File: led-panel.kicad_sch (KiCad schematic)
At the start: 4 parts

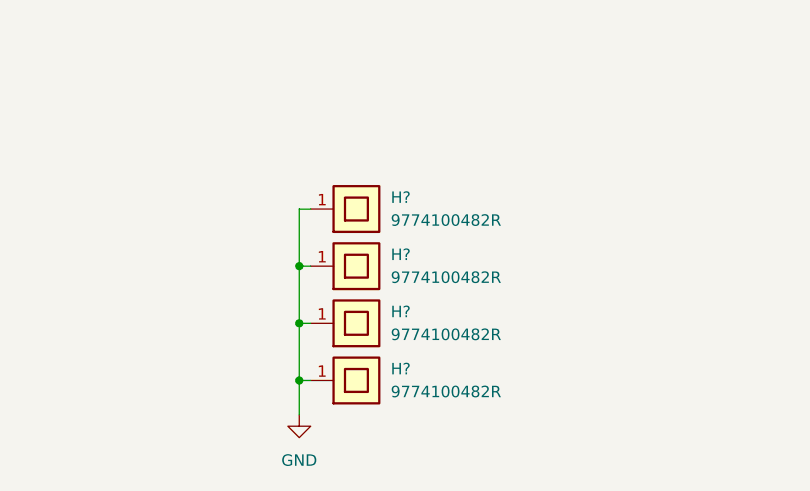
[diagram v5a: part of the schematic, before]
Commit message: [#72133] Change connectors to horizontal
Signed-off-by: Dawid Lentka <dlentka@antmicro.com>
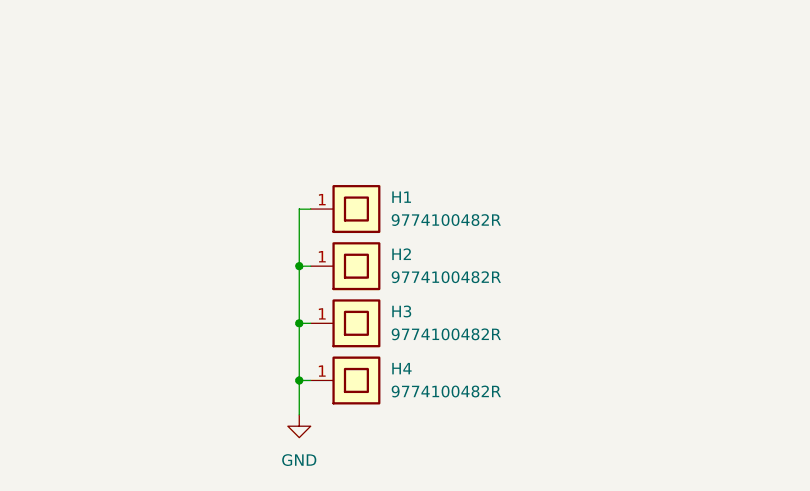
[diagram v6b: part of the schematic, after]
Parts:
- gave numbers to parts that had none: 4
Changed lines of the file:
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@@
 		(dnp no)
 		(fields_autoplaced yes)
-		(property "Reference" "H?"
+		(property "Reference" "H3"
 			(at 160.02 179.07 0)
 			(effects
@@
 			(project "led-panel"
 				(path "/a86e1cab-ea0a-45e6-9194-d44b0d5c9450"
-					(reference "H?")
+					(reference "H3")
 					(unit 1)
 				)
@@
 		(dnp no)
 		(fields_autoplaced yes)
-		(property "Reference" "H?"
+		(property "Reference" "H1"
 			(at 160.02 166.37 0)
 			(effects
@@
 			(project ""
 				(path "/a86e1cab-ea0a-45e6-9194-d44b0d5c9450"
-					(reference "H?")
+					(reference "H1")
 					(unit 1)
 				)
@@
 		(dnp no)
 		(fields_autoplaced yes)
-		(property "Reference" "H?"
+		(property "Reference" "H4"
 			(at 160.02 185.42 0)
 			(effects
@@
 			(project "led-panel"
 				(path "/a86e1cab-ea0a-45e6-9194-d44b0d5c9450"
-					(reference "H?")
+					(reference "H4")
 					(unit 1)
 				)
@@
 		(dnp no)
 		(fields_autoplaced yes)
-		(property "Reference" "H?"
+		(property "Reference" "H2"
 			(at 160.02 172.72 0)
 			(effects
@@
 			(project "led-panel"
 				(path "/a86e1cab-ea0a-45e6-9194-d44b0d5c9450"
-					(reference "H?")
+					(reference "H2")
 					(unit 1)
 				)

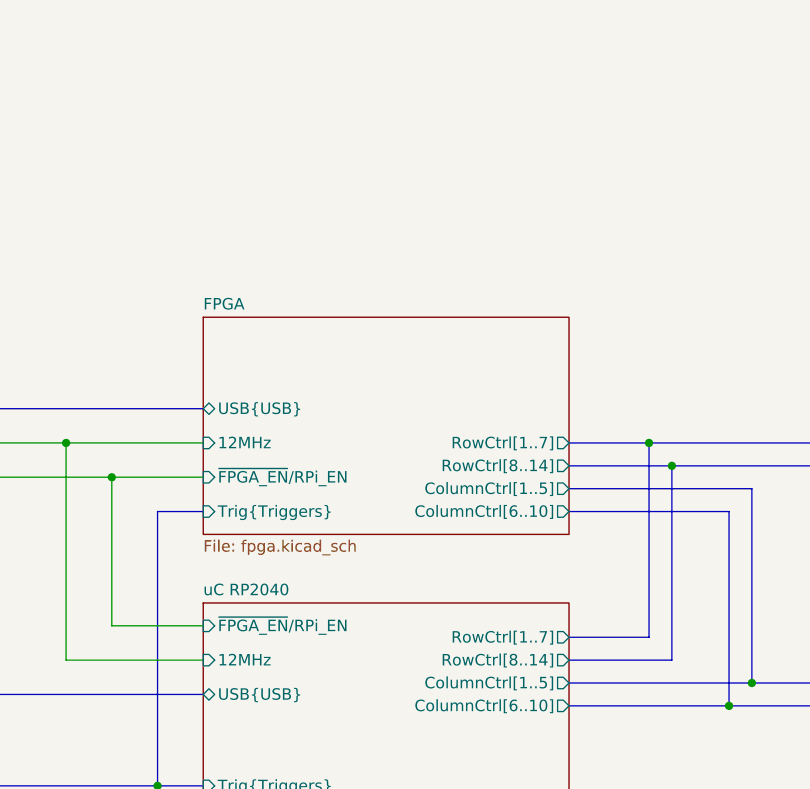
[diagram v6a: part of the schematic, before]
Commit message: [#72133] Sch: Add IMU
Signed-off-by: Dawid Lentka <dlentka@antmicro.com>
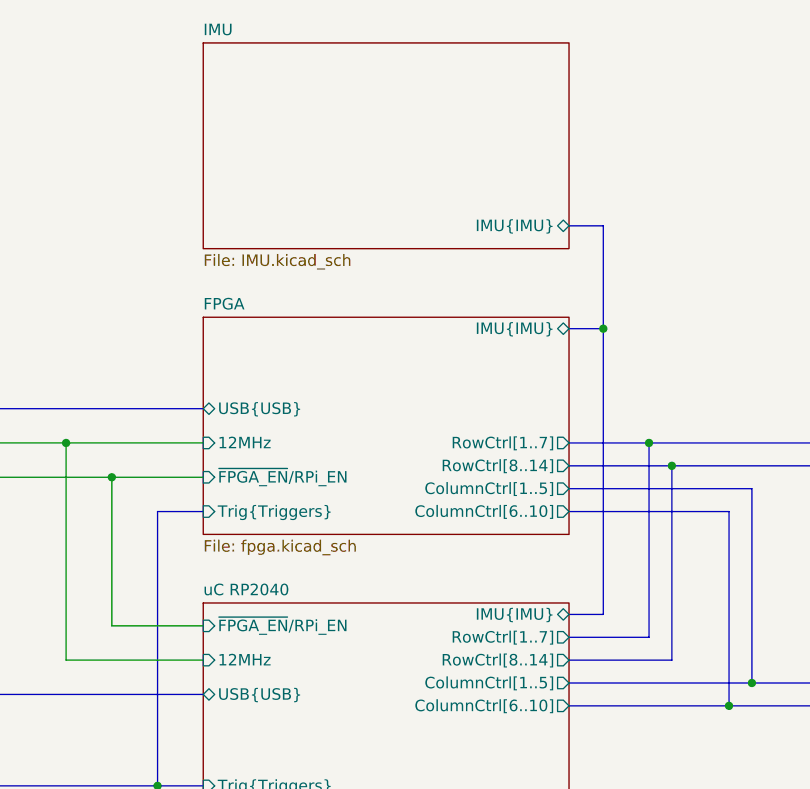
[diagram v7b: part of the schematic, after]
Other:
- added sheet IMU (IMU.kicad_sch)
- sheet FPGA ports: added IMU{IMU}; removed none
- sheet uC RP2040 ports: added IMU{IMU}; removed none
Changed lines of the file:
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@@
+	)
+	(junction
+		(at 165.1 68.58)
+		(diameter 0)
+		(color 0 0 0 0)
 	)
 	(junction
@@
 	(bus
 		(pts
+			(xy 165.1 57.15) (xy 165.1 68.58)
+		)
+		(stroke
+			(width 0)
+			(type default)
+		)
+	)
+	(bus
+		(pts
 			(xy 97.79 77.47) (xy 120.65 77.47)
 		)
@@
 		)
 	)
+	(bus
+		(pts
+			(xy 161.29 57.15) (xy 165.1 57.15)
+		)
+		(stroke
+			(width 0)
+			(type default)
+		)
+	)
 	(wire
 		(pts
@@
 	(bus
 		(pts
+			(xy 165.1 68.58) (xy 165.1 100.33)
+		)
+		(stroke
+			(width 0)
+			(type default)
+		)
+	)
+	(bus
+		(pts
 			(xy 97.79 109.22) (xy 120.65 109.22)
 		)
@@
 	(bus
 		(pts
+			(xy 165.1 100.33) (xy 161.29 100.33)
+		)
+		(stroke
+			(width 0)
+			(type default)
+		)
+	)
+	(bus
+		(pts
 			(xy 53.34 119.38) (xy 58.42 119.38)
 		)
@@
 		(pts
 			(xy 231.14 81.28) (xy 242.57 81.28)
+		)
+		(stroke
+			(width 0)
+			(type default)
+		)
+	)
+	(bus
+		(pts
+			(xy 161.29 68.58) (xy 165.1 68.58)
 		)
 		(stroke
@@
 			)
 		)
+		(pin "IMU{IMU}" bidirectional
+			(at 161.29 100.33 0)
+			(effects
+				(font
+					(size 1.27 1.27)
+				)
+				(justify right)
+			)
+		)
 		(instances
 			(project "led-panel"
@@
 	)
 	(sheet
+		(at 120.65 36.83)
+		(size 40.64 22.86)
+		(fields_autoplaced yes)
+		(stroke
+			(width 0.1524)
+			(type solid)
+		)
+		(fill
+			(color 0 0 0 0.0000)
+		)
+		(property "Sheetname" "IMU"
+			(at 120.65 36.1184 0)
+			(effects
+				(font
+					(size 1.27 1.27)
+				)
+				(justify left bottom)
+			)
+		)
+		(property "Sheetfile" "IMU.kicad_sch"
+			(at 120.65 60.2746 0)
+			(effects
+				(font
+					(size 1.27 1.27)
+				)
+				(justify left top)
+			)
+		)
+		(pin "IMU{IMU}" bidirectional
+			(at 161.29 57.15 0)
+			(effects
+				(font
+					(size 1.27 1.27)
+				)
+				(justify right)
+			)
+		)
+		(instances
+			(project "led-panel"
+				(path "/a86e1cab-ea0a-45e6-9194-d44b0d5c9450"
+					(page "12")
+				)
+			)
+		)
+	)
+	(sheet
 		(at 190.5 99.06)
 		(size 40.64 22.86)
@@
 			(effects
 				(font
+					(size 1.27 1.27)
+				)
+				(justify right)
+			)
+		)
+		(pin "IMU{IMU}" bidirectional
+			(at 161.29 68.58 0)
+			(effects
+				(font

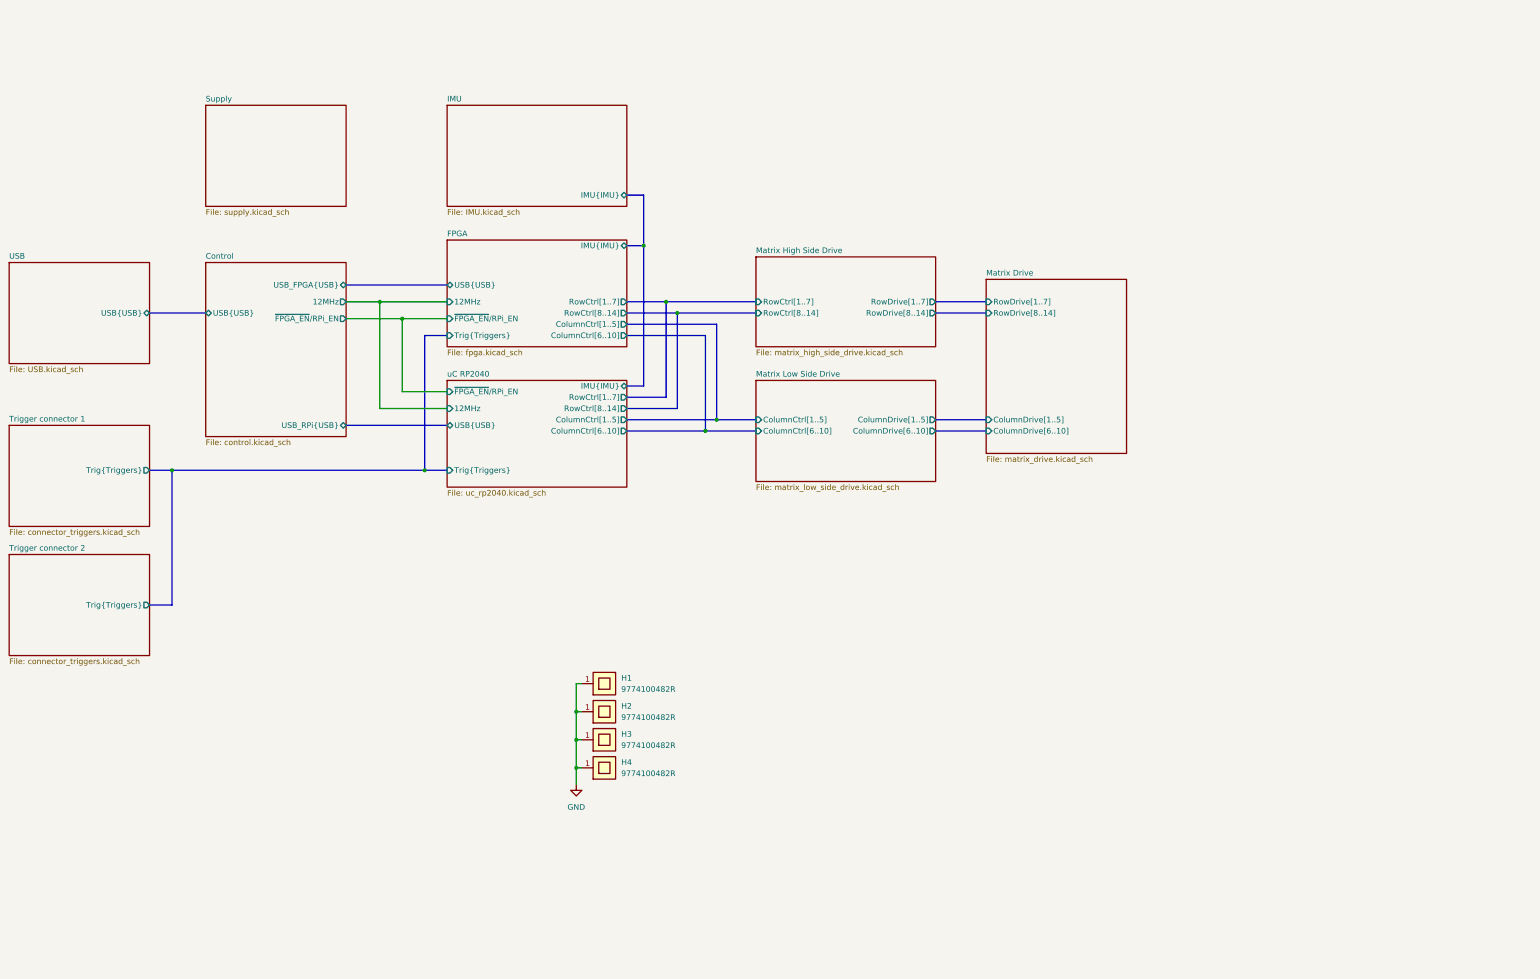
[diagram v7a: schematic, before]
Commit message: [#72133] Sch: Update control hierarchy
Signed-off-by: Dawid Lentka <dlentka@antmicro.com>
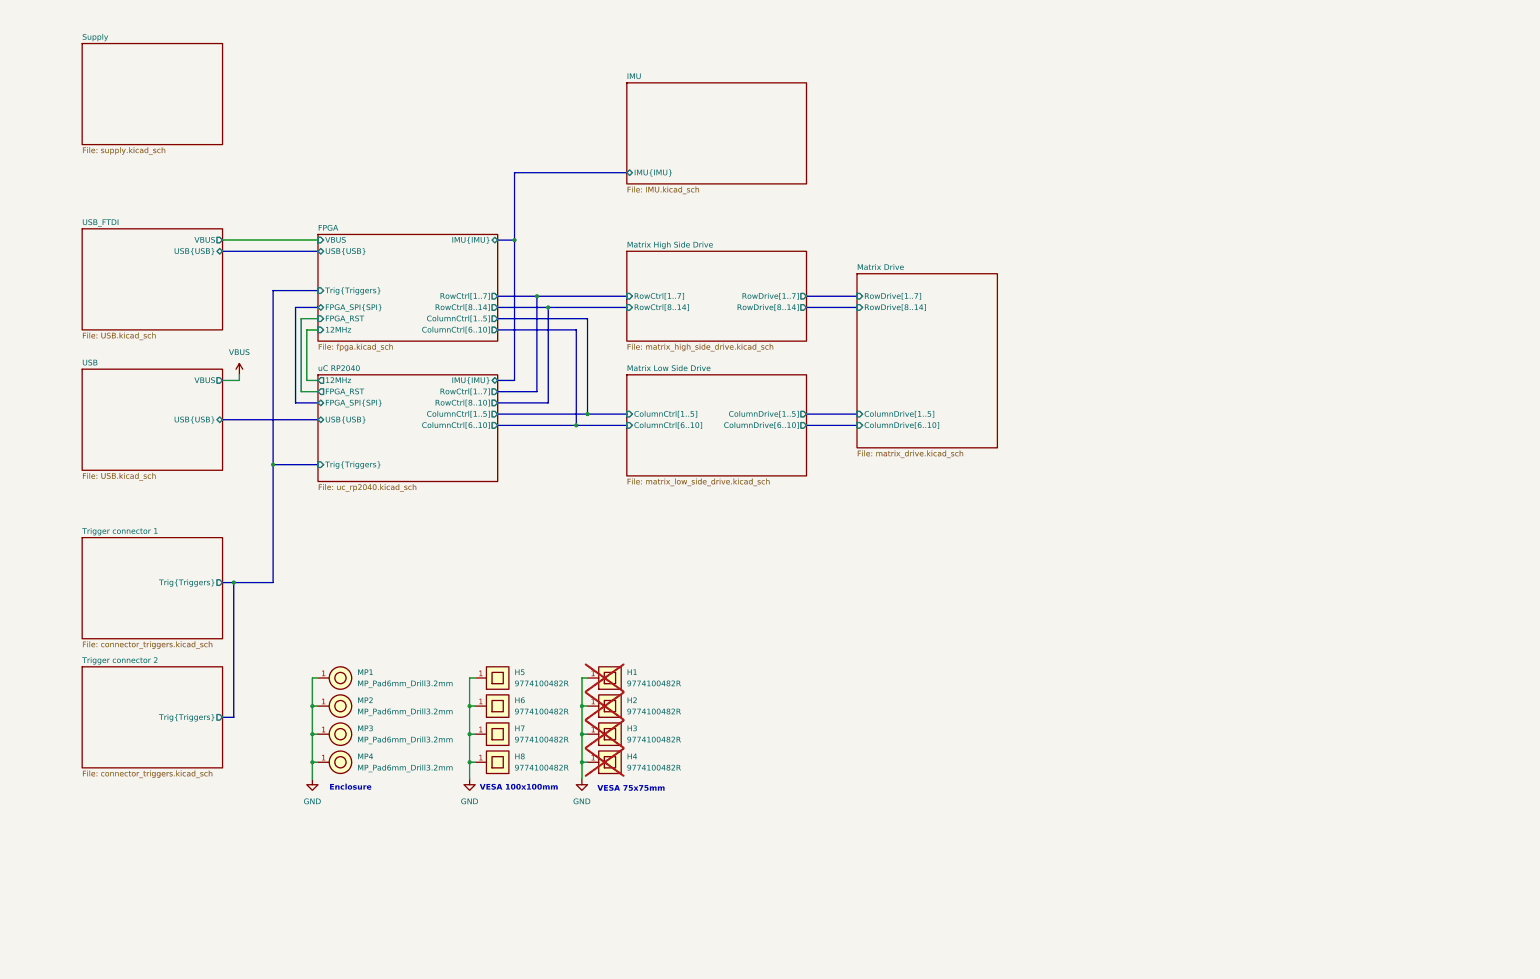
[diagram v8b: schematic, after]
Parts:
- added H5, H6, H7, H8: Spacer_Drill5.4mm_H10mm_9774100482R, antmicro-footprints:Spacer_Drill5.4mm_H10mm_9774100482R, symbol antmicroMechanicalParts:Spacer_Drill5.4mm_H10mm_9774100482R
- added MP1, MP2, MP3, MP4: MP_Pad6mm_Drill3.2mm, antmicro-footprints:MP_Pad6mm_Drill3.2mm, symbol antmicroMechanicalParts:MP_Pad6mm_Drill3.2mm
- H1, H2, H3, H4: now not fitted
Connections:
- net GND: now also H5.1, H6.1, H7.1, H8.1, MP1.1, MP2.1, MP3.1, MP4.1
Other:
- removed sheet Control
- added sheet USB_FTDI (USB.kicad_sch)
- sheet FPGA ports: added FPGA_RST, FPGA_SPI{SPI}, VBUS; removed ~{FPGA_EN}/RPi_EN
- sheet USB ports: added VBUS; removed none
- sheet uC RP2040 ports: added FPGA_RST, FPGA_SPI{SPI}, RowCtrl[8..10]; removed RowCtrl[8..14], ~{FPGA_EN}/RPi_EN
- note added: "Enclosure"
- note added: "VESA 100x100mm"
- note added: "VESA 75x75mm"
